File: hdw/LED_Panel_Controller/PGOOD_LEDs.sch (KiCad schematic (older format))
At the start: 27 parts

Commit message: lots of schematic progress
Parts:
- removed C? (x2): 4.7uF, Capacitors_SMD:C_0805, symbol Custom_Library:C_Custom
- removed Q?: BSS214NW, Package_TO_SOT_SMD:SOT-323_SC-70, symbol Transistor_FET:BSS214NW
- removed R? (x2): 10k, Resistors_SMD:R_0603, symbol Custom_Library:R_Custom
- removed R?: 10, Resistors_SMD:R_0603, symbol Custom_Library:R_Custom
- removed U? (x4): 74LVC1G06, TO_SOT_Packages_SMD:SOT-353_SC-70-5, symbol Custom_Library:74LVC1G06_Power
- removed U?: LP2985-3.3, Package_TO_SOT_SMD:SOT-23-5, symbol Regulator_Linear:LP2985-3.3
- removed U?: 74LVC1G07, TO_SOT_Packages_SMD:SOT-353_SC-70-5, symbol Custom_Library:74LVC1G07_Power
- added R?: 10k, Resistors_SMD:R_0402, symbol Custom_Library:R_Custom
- added U? (x4): 74LVC1G97, Package_TO_SOT_SMD:SOT-363_SC-70-6, symbol Custom_Library:74LVC1G97_Power_NAND_INV
- added U?: 74LVC1G97, Package_TO_SOT_SMD:SOT-363_SC-70-6, symbol Custom_Library:74LVC1G97_Power_AND_INV
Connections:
- net labels added: PGOOD_LED_SHDN
- net labels removed: +12V, +3.3V_PGL, POS3P3_PGL_SHDN
- wire segments 22 -> 13
- no-connect marks 1 -> 0

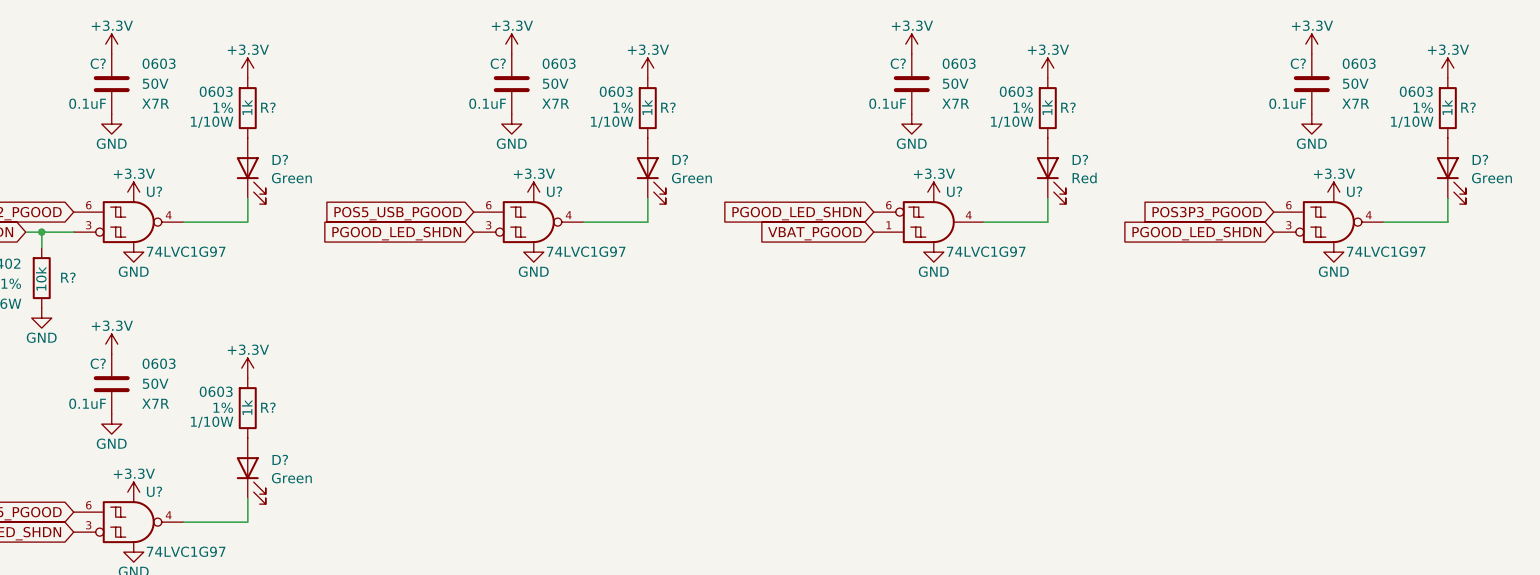
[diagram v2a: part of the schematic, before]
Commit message: added digikey pns, footprints, bom scrubbed
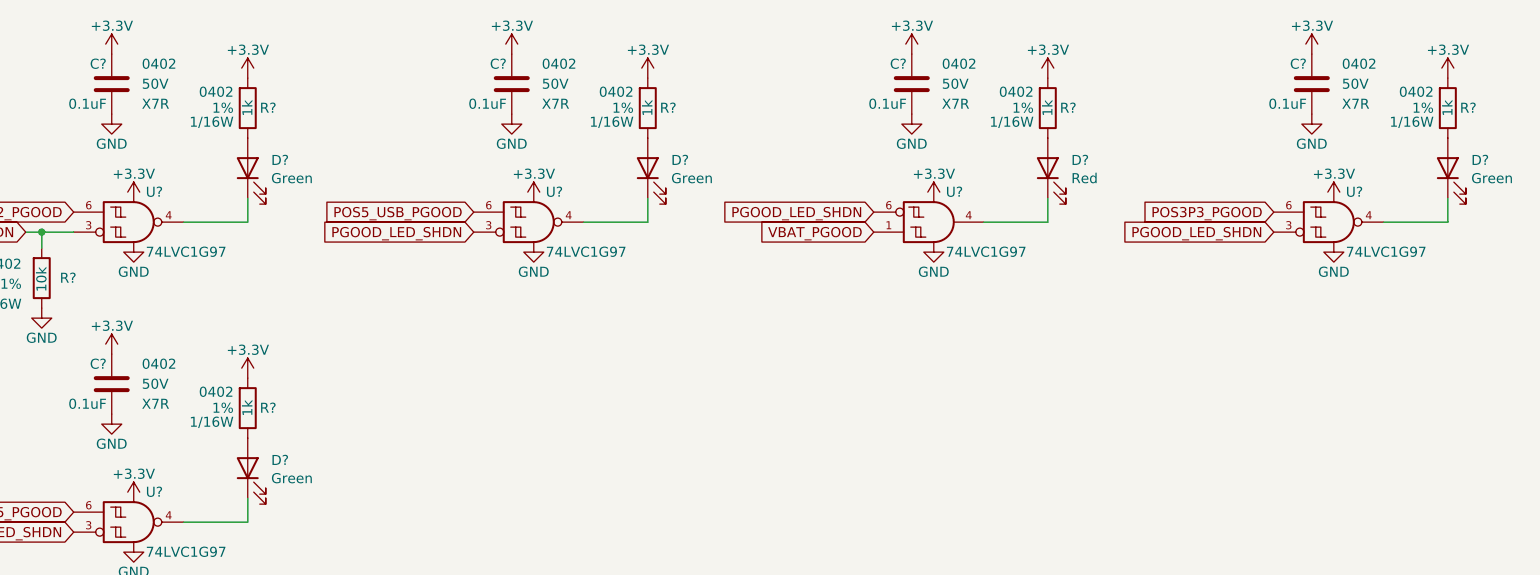
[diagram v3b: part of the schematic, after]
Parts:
- C? (x5): footprint Capacitors_SMD:C_0603 -> Capacitors_SMD:C_0402; Digi-Key PN 399-7845-1-ND -> 490-10701-1-ND; display_footprint 0603 -> 0402
- D? (x4): footprint LEDs:LED_0603 -> LEDs:LED_0402; Digi-Key PN 754-1121-1-ND -> 1497-1219-1-ND
- D?: footprint LEDs:LED_0603 -> LEDs:LED_0402; Digi-Key PN 754-1117-1-ND -> 1497-1174-1-ND
- R? (x5): footprint Resistors_SMD:R_0603 -> Resistors_SMD:R_0402; Digi-Key PN 311-1.00KHRCT-ND -> RMCF0402FT1K00CT-ND; Wattage 1/10W -> 1/16W; display_footprint 0603 -> 0402
- R?: Digi-Key PN (none) -> RMCF0402FT10K0CT-ND
- U? (x5): Digi-Key PN (none) -> 1727-1772-1-ND
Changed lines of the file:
@@
 F 0 "D?" V 3589 2483 50  0000 R CNN
 F 1 "Green" V 3498 2483 50  0000 R CNN
-F 2 "LEDs:LED_0603" H 3550 2600 50  0001 C CNN
+F 2 "LEDs:LED_0402" H 3550 2600 50  0001 C CNN
 F 3 "~" H 3550 2600 50  0001 C CNN
-F 4 "754-1121-1-ND" H -1610 -3720 50  0001 C CNN "Digi-Key PN"
+F 4 "1497-1219-1-ND" H -1610 -3720 50  0001 C CNN "Digi-Key PN"
 	1    3550 2600
 	0    -1   -1   0
@@
 F 0 "R?" H 3490 2300 50  0000 R CNN
 F 1 "1k" V 3550 2300 50  0000 C CNN
-F 2 "Resistors_SMD:R_0603" H 3550 2300 50  0001 C CNN
+F 2 "Resistors_SMD:R_0402" H 3550 2300 50  0001 C CNN
 F 3 "" H 3550 2300 50  0001 C CNN
-F 4 "0603" H 3620 2380 50  0000 L CNN "display_footprint"
+F 4 "0402" H 3620 2380 50  0000 L CNN "display_footprint"
 F 5 "1%" H 3620 2300 50  0000 L CNN "Tolerance"
-F 6 "1/10W" H 3620 2230 50  0000 L CNN "Wattage"
-F 7 "311-1.00KHRCT-ND" H 3850 2700 60  0001 C CNN "Digi-Key PN"
+F 6 "1/16W" H 3620 2230 50  0000 L CNN "Wattage"
+F 7 "RMCF0402FT1K00CT-ND" H 3850 2700 60  0001 C CNN "Digi-Key PN"
 	1    3550 2300
 	-1   0    0    -1
@@
 F 0 "C?" H 8895 2280 50  0000 L CNN
 F 1 "0.1uF" H 8895 2080 50  0000 L CNN
-F 2 "Capacitors_SMD:C_0603" H 8908 2030 50  0001 C CNN
+F 2 "Capacitors_SMD:C_0402" H 8908 2030 50  0001 C CNN
 F 3 "" H 8895 2280 50  0001 C CNN
-F 4 "399-7845-1-ND" H 9295 2680 60  0001 C CNN "Digi-Key PN"
-F 5 "0603" H 8720 2280 50  0000 R CNN "display_footprint"
+F 4 "490-10701-1-ND" H 9295 2680 60  0001 C CNN "Digi-Key PN"
+F 5 "0402" H 8720 2280 50  0000 R CNN "display_footprint"
 F 6 "50V" H 8720 2180 50  0000 R CNN "Voltage"
 F 7 "X7R" H 8720 2080 50  0000 R CNN "Dielectric"
@@
 F 0 "D?" V 9589 2483 50  0000 R CNN
 F 1 "Green" V 9498 2483 50  0000 R CNN
-F 2 "LEDs:LED_0603" H 9550 2600 50  0001 C CNN
+F 2 "LEDs:LED_0402" H 9550 2600 50  0001 C CNN
 F 3 "~" H 9550 2600 50  0001 C CNN
-F 4 "754-1121-1-ND" H 4390 -3720 50  0001 C CNN "Digi-Key PN"
+F 4 "1497-1219-1-ND" H 4390 -3720 50  0001 C CNN "Digi-Key PN"
 	1    9550 2600
 	0    -1   -1   0
@@
 F 0 "R?" H 9490 2300 50  0000 R CNN
 F 1 "1k" V 9550 2300 50  0000 C CNN
-F 2 "Resistors_SMD:R_0603" H 9550 2300 50  0001 C CNN
+F 2 "Resistors_SMD:R_0402" H 9550 2300 50  0001 C CNN
 F 3 "" H 9550 2300 50  0001 C CNN
-F 4 "0603" H 9620 2380 50  0000 L CNN "display_footprint"
+F 4 "0402" H 9620 2380 50  0000 L CNN "display_footprint"
 F 5 "1%" H 9620 2300 50  0000 L CNN "Tolerance"
-F 6 "1/10W" H 9620 2230 50  0000 L CNN "Wattage"
-F 7 "311-1.00KHRCT-ND" H 9850 2700 60  0001 C CNN "Digi-Key PN"
+F 6 "1/16W" H 9620 2230 50  0000 L CNN "Wattage"
+F 7 "RMCF0402FT1K00CT-ND" H 9850 2700 60  0001 C CNN "Digi-Key PN"
 	1    9550 2300
 	-1   0    0    -1
@@
 F 0 "C?" H 6895 2280 50  0000 L CNN
 F 1 "0.1uF" H 6895 2080 50  0000 L CNN
-F 2 "Capacitors_SMD:C_0603" H 6908 2030 50  0001 C CNN
+F 2 "Capacitors_SMD:C_0402" H 6908 2030 50  0001 C CNN
 F 3 "" H 6895 2280 50  0001 C CNN
-F 4 "399-7845-1-ND" H 7295 2680 60  0001 C CNN "Digi-Key PN"
-F 5 "0603" H 6720 2280 50  0000 R CNN "display_footprint"
+F 4 "490-10701-1-ND" H 7295 2680 60  0001 C CNN "Digi-Key PN"
+F 5 "0402" H 6720 2280 50  0000 R CNN "display_footprint"
 F 6 "50V" H 6720 2180 50  0000 R CNN "Voltage"
 F 7 "X7R" H 6720 2080 50  0000 R CNN "Dielectric"
@@
 F 0 "D?" V 7589 2483 50  0000 R CNN
 F 1 "Red" V 7498 2483 50  0000 R CNN
-F 2 "LEDs:LED_0603" H 7550 2600 50  0001 C CNN
+F 2 "LEDs:LED_0402" H 7550 2600 50  0001 C CNN
 F 3 "~" H 7550 2600 50  0001 C CNN
-F 4 "754-1117-1-ND" H 7550 2600 50  0001 C CNN "Digi-Key PN"
+F 4 "1497-1174-1-ND" H 7550 2600 50  0001 C CNN "Digi-Key PN"
 	1    7550 2600
 	0    -1   -1   0
@@
 F 0 "R?" H 7490 2300 50  0000 R CNN
 F 1 "1k" V 7550 2300 50  0000 C CNN
-F 2 "Resistors_SMD:R_0603" H 7550 2300 50  0001 C CNN
+F 2 "Resistors_SMD:R_0402" H 7550 2300 50  0001 C CNN
 F 3 "" H 7550 2300 50  0001 C CNN
-F 4 "0603" H 7620 2380 50  0000 L CNN "display_footprint"
+F 4 "0402" H 7620 2380 50  0000 L CNN "display_footprint"
 F 5 "1%" H 7620 2300 50  0000 L CNN "Tolerance"
-F 6 "1/10W" H 7620 2230 50  0000 L CNN "Wattage"
-F 7 "311-1.00KHRCT-ND" H 7850 2700 60  0001 C CNN "Digi-Key PN"
+F 6 "1/16W" H 7620 2230 50  0000 L CNN "Wattage"
+F 7 "RMCF0402FT1K00CT-ND" H 7850 2700 60  0001 C CNN "Digi-Key PN"
 	1    7550 2300
 	-1   0    0    -1
@@
 F 0 "C?" H 2895 2280 50  0000 L CNN
 F 1 "0.1uF" H 2895 2080 50  0000 L CNN
-F 2 "Capacitors_SMD:C_0603" H 2908 2030 50  0001 C CNN
+F 2 "Capacitors_SMD:C_0402" H 2908 2030 50  0001 C CNN
 F 3 "" H 2895 2280 50  0001 C CNN
-F 4 "399-7845-1-ND" H 3295 2680 60  0001 C CNN "Digi-Key PN"
-F 5 "0603" H 2720 2280 50  0000 R CNN "display_footprint"
+F 4 "490-10701-1-ND" H 3295 2680 60  0001 C CNN "Digi-Key PN"
+F 5 "0402" H 2720 2280 50  0000 R CNN "display_footprint"
 F 6 "50V" H 2720 2180 50  0000 R CNN "Voltage"
 F 7 "X7R" H 2720 2080 50  0000 R CNN "Dielectric"
@@
 F 0 "R?" H 3490 3800 50  0000 R CNN
 F 1 "1k" V 3550 3800 50  0000 C CNN
-F 2 "Resistors_SMD:R_0603" H 3550 3800 50  0001 C CNN
+F 2 "Resistors_SMD:R_0402" H 3550 3800 50  0001 C CNN
 F 3 "" H 3550 3800 50  0001 C CNN
-F 4 "0603" H 3620 3880 50  0000 L CNN "display_footprint"
+F 4 "0402" H 3620 3880 50  0000 L CNN "display_footprint"
 F 5 "1%" H 3620 3800 50  0000 L CNN "Tolerance"
-F 6 "1/10W" H 3620 3730 50  0000 L CNN "Wattage"
-F 7 "311-1.00KHRCT-ND" H 3850 4200 60  0001 C CNN "Digi-Key PN"
+F 6 "1/16W" H 3620 3730 50  0000 L CNN "Wattage"
+F 7 "RMCF0402FT1K00CT-ND" H 3850 4200 60  0001 C CNN "Digi-Key PN"
 	1    3550 3800
 	-1   0    0    -1
@@
 F 0 "D?" V 3589 3983 50  0000 R CNN
 F 1 "Green" V 3498 3983 50  0000 R CNN
-F 2 "LEDs:LED_0603" H 3550 4100 50  0001 C CNN
+F 2 "LEDs:LED_0402" H 3550 4100 50  0001 C CNN
 F 3 "~" H 3550 4100 50  0001 C CNN
-F 4 "754-1121-1-ND" H -1610 -2220 50  0001 C CNN "Digi-Key PN"
+F 4 "1497-1219-1-ND" H -1610 -2220 50  0001 C CNN "Digi-Key PN"
 	1    3550 4100
 	0    -1   -1   0
@@
 F 0 "C?" H 2895 3780 50  0000 L CNN
 F 1 "0.1uF" H 2895 3580 50  0000 L CNN
-F 2 "Capacitors_SMD:C_0603" H 2908 3530 50  0001 C CNN
+F 2 "Capacitors_SMD:C_0402" H 2908 3530 50  0001 C CNN
 F 3 "" H 2895 3780 50  0001 C CNN
-F 4 "399-7845-1-ND" H 3295 4180 60  0001 C CNN "Digi-Key PN"
-F 5 "0603" H 2720 3780 50  0000 R CNN "display_footprint"
+F 4 "490-10701-1-ND" H 3295 4180 60  0001 C CNN "Digi-Key PN"
+F 5 "0402" H 2720 3780 50  0000 R CNN "display_footprint"
 F 6 "50V" H 2720 3680 50  0000 R CNN "Voltage"
 F 7 "X7R" H 2720 3580 50  0000 R CNN "Dielectric"
@@
 F 0 "R?" H 5490 2300 50  0000 R CNN
 F 1 "1k" V 5550 2300 50  0000 C CNN
-F 2 "Resistors_SMD:R_0603" H 5550 2300 50  0001 C CNN
+F 2 "Resistors_SMD:R_0402" H 5550 2300 50  0001 C CNN
 F 3 "" H 5550 2300 50  0001 C CNN
-F 4 "0603" H 5620 2380 50  0000 L CNN "display_footprint"
+F 4 "0402" H 5620 2380 50  0000 L CNN "display_footprint"
 F 5 "1%" H 5620 2300 50  0000 L CNN "Tolerance"
-F 6 "1/10W" H 5620 2230 50  0000 L CNN "Wattage"
-F 7 "311-1.00KHRCT-ND" H 5850 2700 60  0001 C CNN "Digi-Key PN"
+F 6 "1/16W" H 5620 2230 50  0000 L CNN "Wattage"
+F 7 "RMCF0402FT1K00CT-ND" H 5850 2700 60  0001 C CNN "Digi-Key PN"
 	1    5550 2300
 	-1   0    0    -1
@@
 F 0 "D?" V 5589 2483 50  0000 R CNN
 F 1 "Green" V 5498 2483 50  0000 R CNN
-F 2 "LEDs:LED_0603" H 5550 2600 50  0001 C CNN
+F 2 "LEDs:LED_0402" H 5550 2600 50  0001 C CNN
 F 3 "~" H 5550 2600 50  0001 C CNN
-F 4 "754-1121-1-ND" H 390 -3720 50  0001 C CNN "Digi-Key PN"
+F 4 "1497-1219-1-ND" H 390 -3720 50  0001 C CNN "Digi-Key PN"
 	1    5550 2600
 	0    -1   -1   0
@@
 F 0 "C?" H 4895 2280 50  0000 L CNN
 F 1 "0.1uF" H 4895 2080 50  0000 L CNN
-F 2 "Capacitors_SMD:C_0603" H 4908 2030 50  0001 C CNN
+F 2 "Capacitors_SMD:C_0402" H 4908 2030 50  0001 C CNN
 F 3 "" H 4895 2280 50  0001 C CNN
-F 4 "399-7845-1-ND" H 5295 2680 60  0001 C CNN "Digi-Key PN"
-F 5 "0603" H 4720 2280 50  0000 R CNN "display_footprint"
+F 4 "490-10701-1-ND" H 5295 2680 60  0001 C CNN "Digi-Key PN"
+F 5 "0402" H 4720 2280 50  0000 R CNN "display_footprint"
 F 6 "50V" H 4720 2180 50  0000 R CNN "Voltage"
 F 7 "X7R" H 4720 2080 50  0000 R CNN "Dielectric"
@@
 F 2 "Package_TO_SOT_SMD:SOT-363_SC-70-6" H 3030 2870 50  0001 C CNN
 F 3 "http://www.ti.com/lit/ds/symlink/sn74lvc1g97.pdf" H 3030 2870 50  0001 C CNN
+F 4 "1727-1772-1-ND" H 2980 2870 50  0001 C CNN "Digi-Key PN"
 	1    2980 2870
 	1    0    0    -1
@@
 F 2 "Package_TO_SOT_SMD:SOT-363_SC-70-6" H 3030 4370 50  0001 C CNN
 F 3 "http://www.ti.com/lit/ds/symlink/sn74lvc1g97.pdf" H 3030 4370 50  0001 C CNN
+F 4 "1727-1772-1-ND" H 2980 4370 50  0001 C CNN "Digi-Key PN"
 	1    2980 4370
 	1    0    0    -1
@@
 F 2 "Package_TO_SOT_SMD:SOT-363_SC-70-6" H 5030 2870 50  0001 C CNN
 F 3 "http://www.ti.com/lit/ds/symlink/sn74lvc1g97.pdf" H 5030 2870 50  0001 C CNN
+F 4 "1727-1772-1-ND" H 4980 2870 50  0001 C CNN "Digi-Key PN"
 	1    4980 2870
 	1    0    0    -1
@@
 F 2 "Package_TO_SOT_SMD:SOT-363_SC-70-6" H 9030 2870 50  0001 C CNN
 F 3 "http://www.ti.com/lit/ds/symlink/sn74lvc1g97.pdf" H 9030 2870 50  0001 C CNN
+F 4 "1727-1772-1-ND" H 8980 2870 50  0001 C CNN "Digi-Key PN"
 	1    8980 2870
 	1    0    0    -1
@@
 F 2 "Package_TO_SOT_SMD:SOT-363_SC-70-6" H 7030 2870 50  0001 C CNN
 F 3 "http://www.ti.com/lit/ds/symlink/sn74lvc1g97.pdf" H 7030 2870 50  0001 C CNN
+F 4 "1727-1772-1-ND" H 6980 2870 50  0001 C CNN "Digi-Key PN"
 	1    6980 2870
 	1    0    0    -1
@@
 F 5 "1%" H 2620 3120 50  0000 L CNN "Tolerance"
 F 6 "1/16W" H 2620 3020 50  0000 L CNN "Wattage"
-F 7 "" H 2820 3550 60  0001 C CNN "Digi-Key PN"
+F 7 "RMCF0402FT10K0CT-ND" H 2820 3550 60  0001 C CNN "Digi-Key PN"
 	1    2520 3150
 	-1   0    0    -1

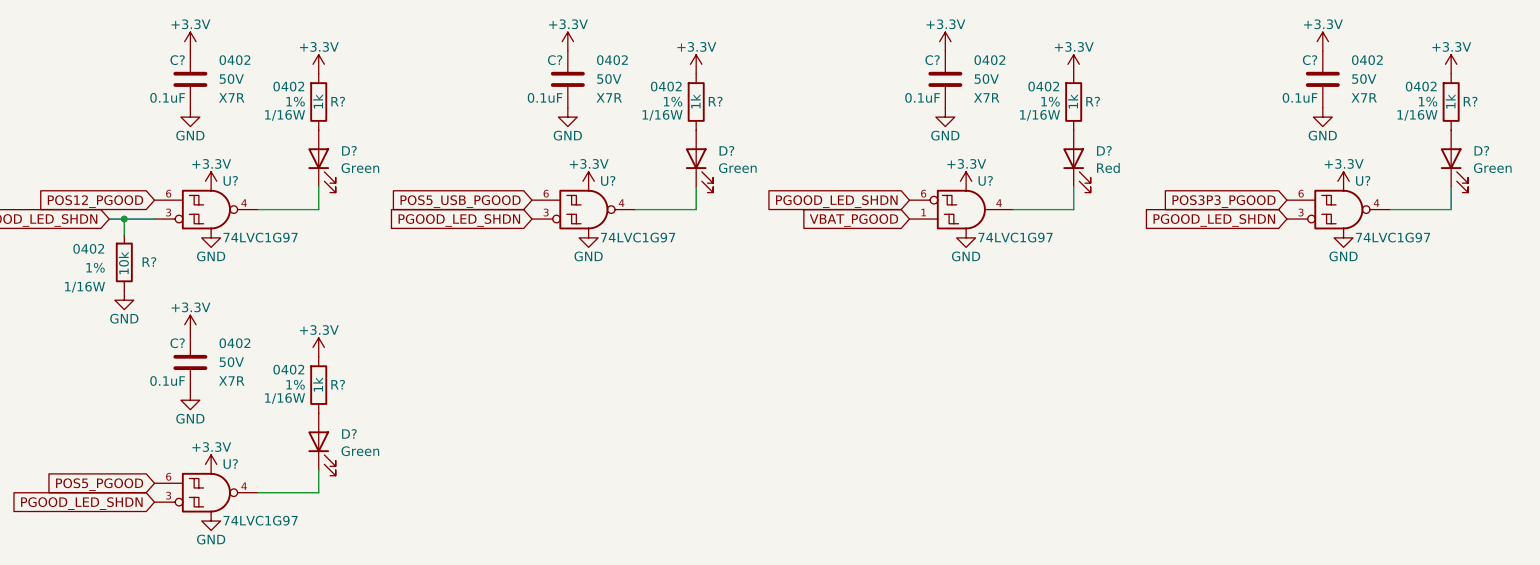
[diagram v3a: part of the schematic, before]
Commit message: assigned I2C addresses
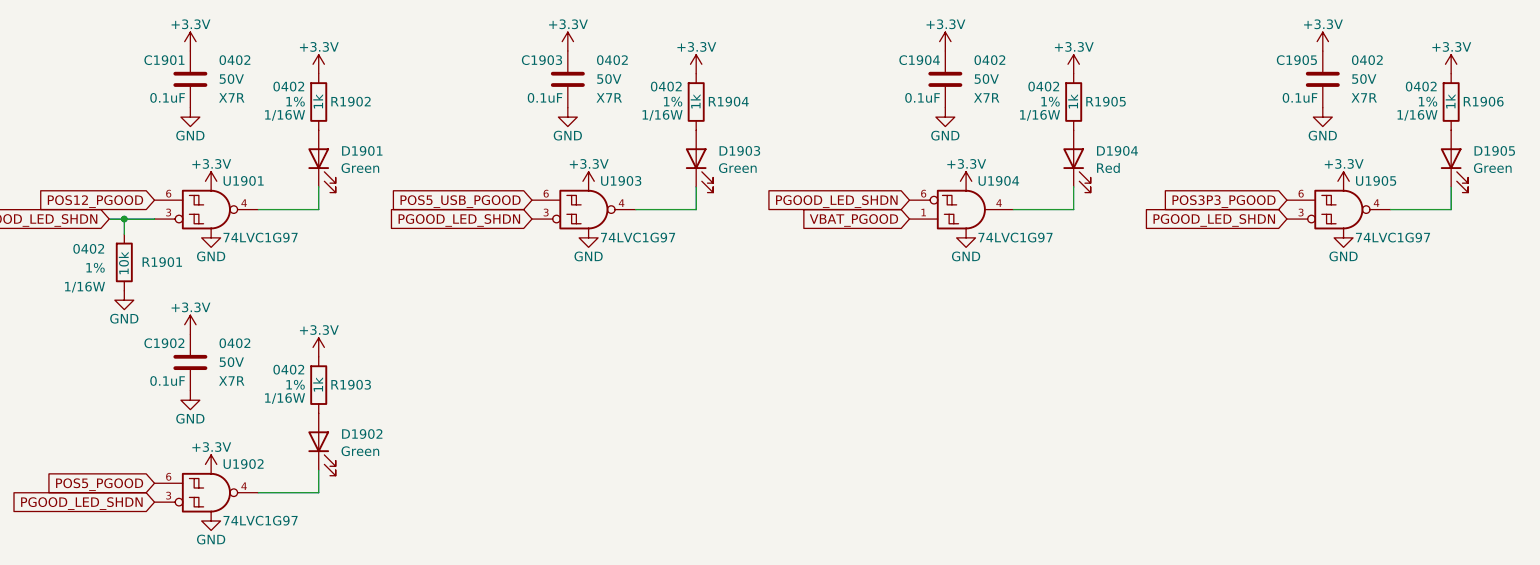
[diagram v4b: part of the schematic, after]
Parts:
- gave numbers to parts that had none: 21

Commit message: added BOMs, some consolidation
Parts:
- C1901, C1902, C1903, C1904, C1905: Digi-Key PN 490-10701-1-ND -> 490-10698-1-ND
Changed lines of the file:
@@
 F 2 "Capacitors_SMD:C_0402" H 8908 2030 50  0001 C CNN
 F 3 "" H 8895 2280 50  0001 C CNN
-F 4 "490-10701-1-ND" H 9295 2680 60  0001 C CNN "Digi-Key PN"
+F 4 "490-10698-1-ND" H 9295 2680 60  0001 C CNN "Digi-Key PN"
 F 5 "0402" H 8720 2280 50  0000 R CNN "display_footprint"
 F 6 "50V" H 8720 2180 50  0000 R CNN "Voltage"
@@
 F 2 "Capacitors_SMD:C_0402" H 6908 2030 50  0001 C CNN
 F 3 "" H 6895 2280 50  0001 C CNN
-F 4 "490-10701-1-ND" H 7295 2680 60  0001 C CNN "Digi-Key PN"
+F 4 "490-10698-1-ND" H 7295 2680 60  0001 C CNN "Digi-Key PN"
 F 5 "0402" H 6720 2280 50  0000 R CNN "display_footprint"
 F 6 "50V" H 6720 2180 50  0000 R CNN "Voltage"
@@
 F 2 "Capacitors_SMD:C_0402" H 2908 2030 50  0001 C CNN
 F 3 "" H 2895 2280 50  0001 C CNN
-F 4 "490-10701-1-ND" H 3295 2680 60  0001 C CNN "Digi-Key PN"
+F 4 "490-10698-1-ND" H 3295 2680 60  0001 C CNN "Digi-Key PN"
 F 5 "0402" H 2720 2280 50  0000 R CNN "display_footprint"
 F 6 "50V" H 2720 2180 50  0000 R CNN "Voltage"
@@
 F 2 "Capacitors_SMD:C_0402" H 2908 3530 50  0001 C CNN
 F 3 "" H 2895 3780 50  0001 C CNN
-F 4 "490-10701-1-ND" H 3295 4180 60  0001 C CNN "Digi-Key PN"
+F 4 "490-10698-1-ND" H 3295 4180 60  0001 C CNN "Digi-Key PN"
 F 5 "0402" H 2720 3780 50  0000 R CNN "display_footprint"
 F 6 "50V" H 2720 3680 50  0000 R CNN "Voltage"
@@
 F 2 "Capacitors_SMD:C_0402" H 4908 2030 50  0001 C CNN
 F 3 "" H 4895 2280 50  0001 C CNN
-F 4 "490-10701-1-ND" H 5295 2680 60  0001 C CNN "Digi-Key PN"
+F 4 "490-10698-1-ND" H 5295 2680 60  0001 C CNN "Digi-Key PN"
 F 5 "0402" H 4720 2280 50  0000 R CNN "display_footprint"
 F 6 "50V" H 4720 2180 50  0000 R CNN "Voltage"
